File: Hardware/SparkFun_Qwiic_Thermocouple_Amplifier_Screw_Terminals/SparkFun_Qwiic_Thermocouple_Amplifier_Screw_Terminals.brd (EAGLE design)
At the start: 25.4 x 25.4 mm, 53 parts, among them J1 PTH, J2 QWIIC, J3 QWIIC, U1 MCP9600-SMD

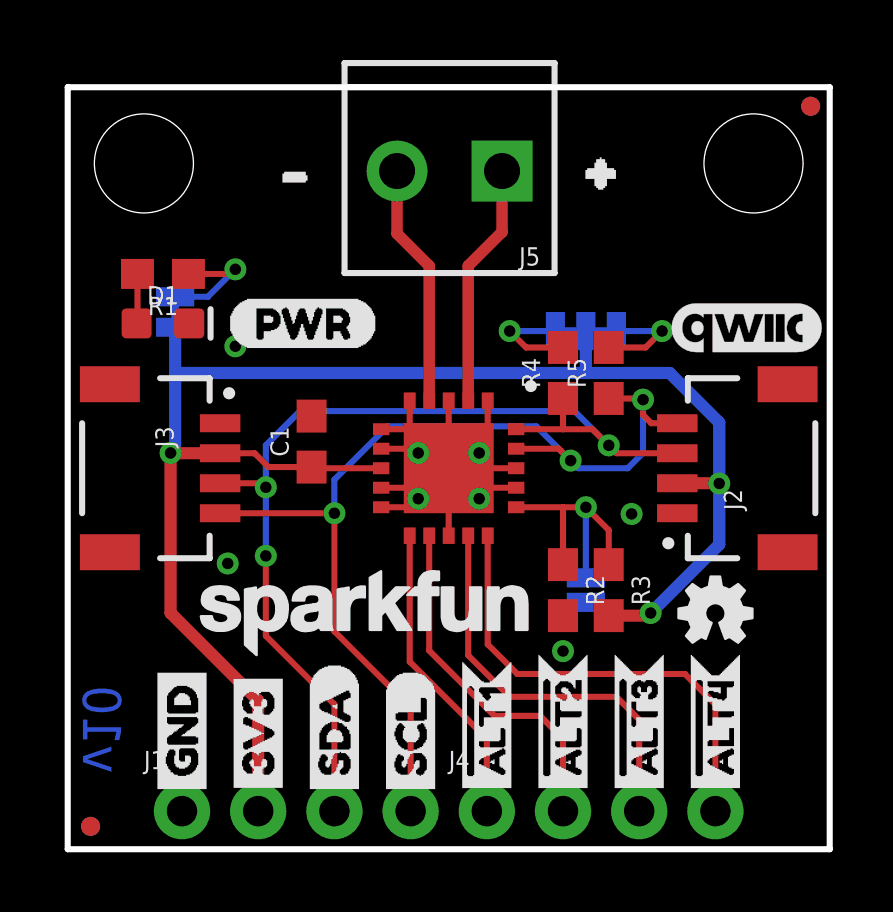
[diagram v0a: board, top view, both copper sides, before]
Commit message: Design review changes
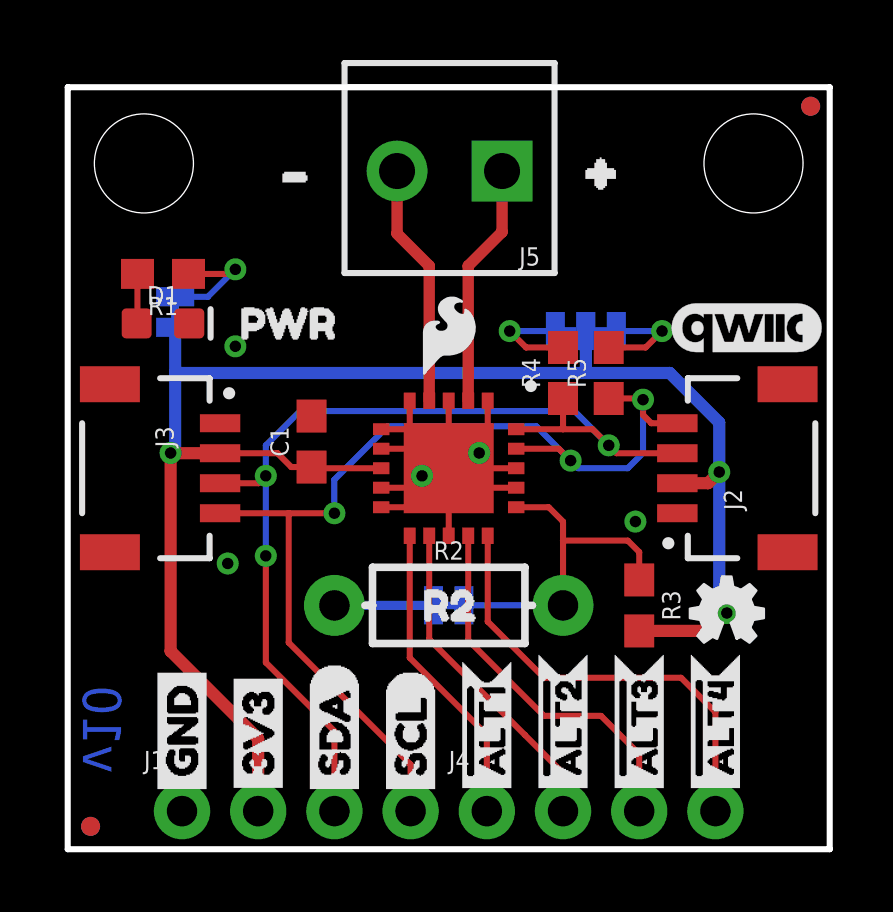
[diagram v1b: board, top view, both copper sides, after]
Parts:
- added U$28: (no value), buzzard_labels (9):ADDR1
- JP1: device SparkFun-Jumpers:SMT-JUMPER_2_NO_SILK -> SparkFun-Jumpers:SMT-JUMPER_2_NC_TRACE_SILK
- LOGO2: value SFE_LOGO_NAME.1_INCH -> SFE_LOGO_NAME_FLAME.1_INCH; device SparkFun-Aesthetics:SFE_LOGO_NAME_.1 -> SparkFun-Aesthetics:SFE_LOGO_NAME_FLAME_.1
- R2: value 43k -> (none); device SparkFun-Resistors:0603 -> SparkFun-Resistors:AXIAL-0.3-KIT
- U$10: device buzzard_labels (7):ADR_#_0X660 -> buzzard_labels (8):R21
- U$23: device buzzard_labels (1):ADR_#_0X600 -> SparkFun-Aesthetics:SFE_LOGO_FLAME_.1
- U$9: device buzzard_labels:PWR8 -> buzzard_labels (8):PWR0
- moved U$23 9.43 mm to (12.7, 17.1), flipped to the top
- moved U$26 9.12 mm to (24.5, 11.9)
- moved LOGO2 7.41 mm to (12.7, 14.7), flipped to the bottom
- moved U$10 6.27 mm to (10.9, 8.13), flipped to the top
- moved JP1 4.60 mm to (12.7, 8.13), turned to 0 degrees
- moved R2 3.84 mm to (12.7, 8.13), turned to 0 degrees
- moved U$25 3.56 mm to (19.2, 19.1)
- moved U$27 2.22 mm to (9.78, 11.9)
- moved R3 1.14 mm to (19.1, 8.13)
- moved U$9 0.51 mm to (4.83, 17.5)
- moved LOGO1 0.38 mm to (22.0, 7.87)
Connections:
- net ADDR: now also R2.P$2; no longer R2.1
- net GND: now also R2.P$1; no longer R2.2
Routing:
- net GND: track 23.6 -> 27.5 mm, vias 8 -> 5
- net ADDR: track 8.82 -> 11.5 mm, vias 1 -> 0
- net 3.3V: track 55.0 -> 56.0 mm
- net !ALT3: track 13.6 -> 12.7 mm
- net !ALT2: track 11.9 -> 11.0 mm
- net SCL: track 34.4 -> 35.0 mm
- net !ALT4: track 15.6 -> 15.0 mm
